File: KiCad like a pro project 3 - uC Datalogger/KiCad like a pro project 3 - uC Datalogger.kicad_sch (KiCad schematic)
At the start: 25 parts, among them U1 24LC1025, U2 24LC1025, U3 DS1337S+, U4 ATMEGA328P_VQFNVQFN, Y1 32.768 KHz, Y2 16 MHz

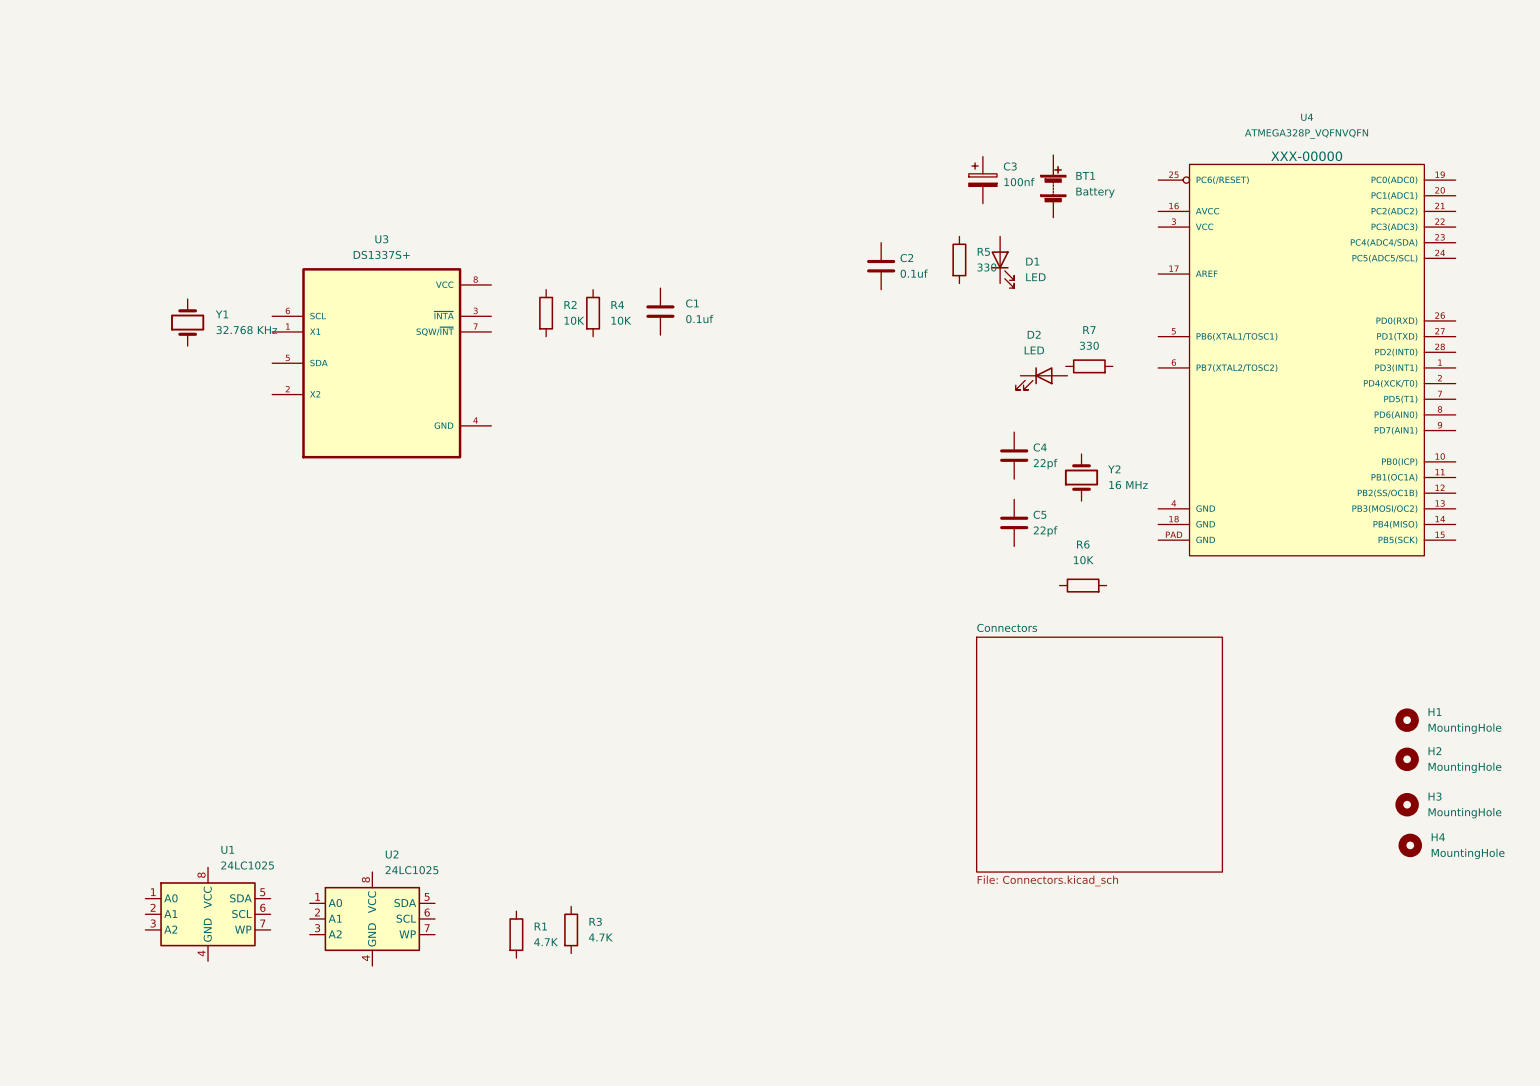
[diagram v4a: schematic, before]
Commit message: Completed wiring of main sheet
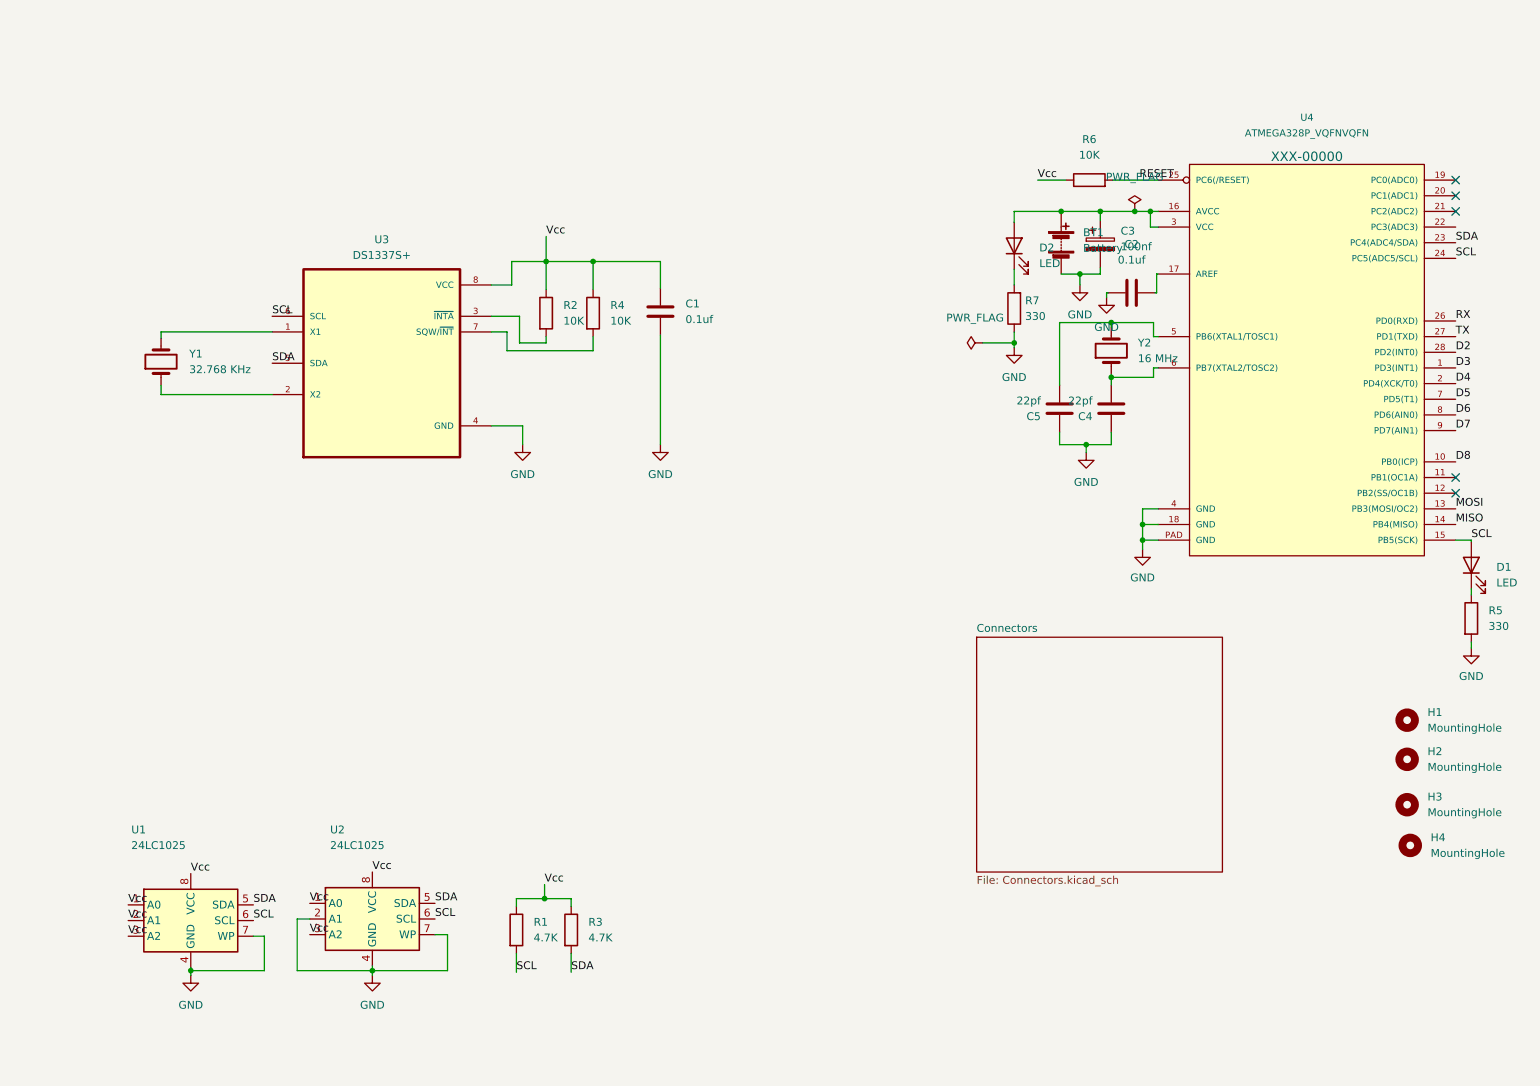
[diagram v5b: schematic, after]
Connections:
- net at D1.1 (K): now also R5.1
- net SCL: now reaches D1.2 (A)
- net SCL: now also R1.2, U1.6 (SCL), U2.6 (SCL), U3.6 (SCL), U4.15 (PB5(SCK)), U4.24 (PC5(ADC5/SCL))
- net at U3.1 (X1): now also Y1.2
- net at U3.2 (X2): now also Y1.1
- net at U3.3 (~{INTA}): now also R2.2
- net GND: now reaches U3.4 (GND)
- net GND: now also BT1.2 (-), C1.2, C2.1, C3.2, C4.1, C5.1, R5.2, R7.1, U1.4 (GND), U1.7 (WP), U2.2 (A1), U2.4 (GND), U2.7 (WP), U4.18 (GND), U4.4 (GND), U4.PAD (GND)
- net SDA: now reaches U3.5 (SDA)
- net SDA: now also R3.2, U1.5 (SDA), U2.5 (SDA), U4.23 (PC4(ADC4/SDA))
- net at U3.7 (SQW/~{INT}): now also R4.2
- net Vcc: now reaches U3.8 (VCC)
- net Vcc: now also C1.1, R1.1, R2.1, R3.1, R4.1, R6.1, U1.1 (A0), U1.2 (A1), U1.3 (A2), U1.8 (VCC), U2.1 (A0), U2.3 (A2), U2.8 (VCC)
- net at C5.2: now also U4.5 (PB6(XTAL1/TOSC1)), Y2.2
- net RESET: now reaches R6.2
- net RESET: now also U4.25 (PC6(/RESET))
- net at C3.1: now also BT1.1 (+), D2.2 (A), U4.16 (AVCC), U4.3 (VCC)
- net at R7.2: now also D2.1 (K)
- net D3: now reaches U4.1 (PD3(INT1))
- net D8: now reaches U4.10 (PB0(ICP))
- net MOSI: now reaches U4.13 (PB3(MOSI/OC2))
- net MISO: now reaches U4.14 (PB4(MISO))
- net at U4.17 (AREF): now also C2.2
- net D4: now reaches U4.2 (PD4(XCK/T0))
- net RX: now reaches U4.26 (PD0(RXD))
- net TX: now reaches U4.27 (PD1(TXD))
- net D2: now reaches U4.28 (PD2(INT0))
- net at U4.6 (PB7(XTAL2/TOSC2)): now also C4.2, Y2.1
- net D5: now reaches U4.7 (PD5(T1))
- net D6: now reaches U4.8 (PD6(AIN0))
- net D7: now reaches U4.9 (PD7(AIN1))
- no-connect marks 0 -> 5
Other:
- moved on the sheet: BT1, C2, C3, C4, C5, D1, D2, R1, R5, R6, R7, U1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

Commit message: finished wiring on connector sheet
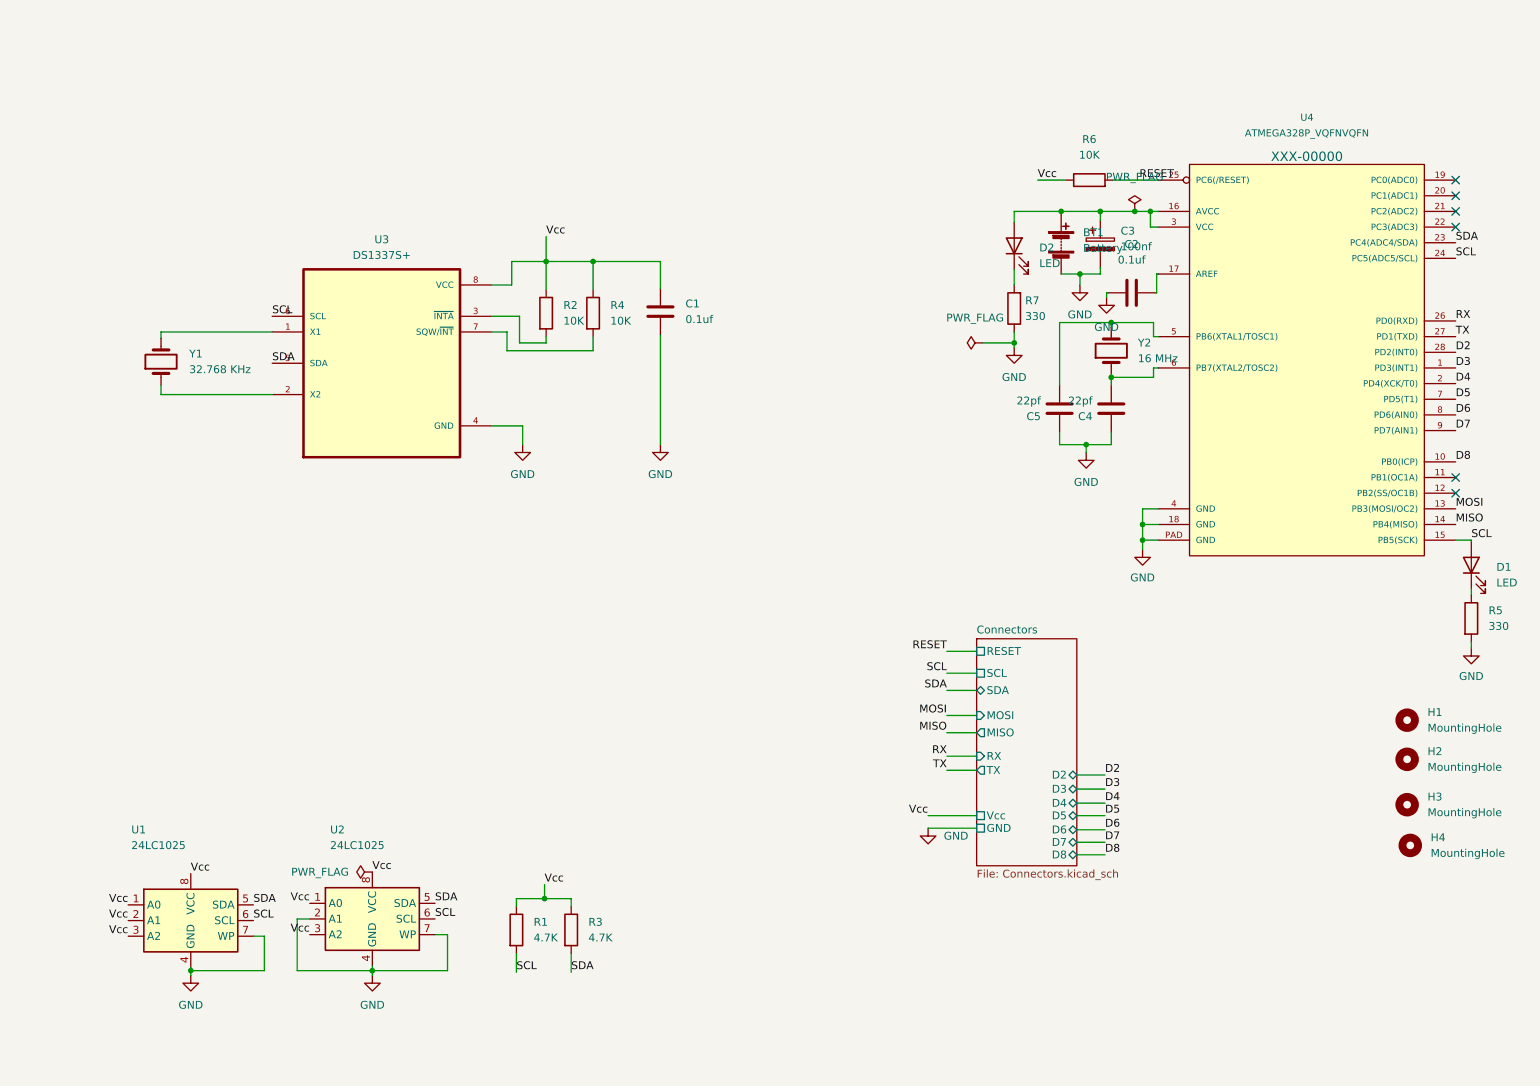
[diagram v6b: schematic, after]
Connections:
- no-connect marks 5 -> 6
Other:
- sheet Connectors ports: added D2, D3, D4, D5, D6, D7, D8, GND, MISO, MOSI, RESET, RX, SCL, SDA, TX, Vcc; removed none

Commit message: Completed comments
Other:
- note added: "Clock"
- note added: "Connectors"
- note added: "EEPROM"
- note added: "MCU"
- note added: "Mounting Holes"
- moved on the sheet: H1, H2, H3, H4, R1, R3, U1, U2
